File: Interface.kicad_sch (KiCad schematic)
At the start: 14 parts, among them J1 Debugger, J2 USART, J3 SPI, P1 USB_C_Plug_USB2.0

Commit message: change pin default and try layout
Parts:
- removed P1: USB_C_Plug_USB2.0, Connector_USB:USB_C_Receptacle_HRO_TYPE-C-31-M-12, symbol Connector:USB_C_Plug_USB2.0
- removed R10, R9: 20, Resistor_SMD:R_0603_1608Metric, symbol Device:R_Small
- removed R11: 1.5K, Resistor_SMD:R_0603_1608Metric, symbol Device:R_Small
- added J4: USB_C_Receptacle_USB2.0, Connector_USB:USB_C_Receptacle_HRO_TYPE-C-31-M-12, symbol Connector:USB_C_Receptacle_USB2.0
- added U3: USBLC6-2SC6, Package_TO_SOT_SMD:SOT-23-6, symbol Power_Protection:USBLC6-2SC6
- R25: value 0 -> 5.1K
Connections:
- net D+: now also U3.4 (I/O2)
- net D-: now also U3.6 (I/O1)
- net GND: now also J4.A1 (GND), J4.A12 (GND), J4.B1 (GND), J4.B12 (GND), J4.S1 (SHIELD), U3.2 (GND)
- net MISO: now also J3.2 (Pin_2); no longer J3.3 (Pin_3)
- net MOSI: now also J3.3 (Pin_3); no longer J3.4 (Pin_4)
- net SCK: now also J3.4 (Pin_4); no longer J3.2 (Pin_2)
- net VIN: now also J4.A4 (VBUS), J4.A9 (VBUS), J4.B4 (VBUS), J4.B9 (VBUS), U3.5 (VBUS)
- net at R25.1: now also J4.B5 (CC2)
- net at R24.1: now also J4.A5 (CC1)
- new net: J4.A7 (D-), J4.B7 (D-), U3.1 (I/O1)
- new net: J4.A6 (D+), J4.B6 (D+), U3.3 (I/O2)

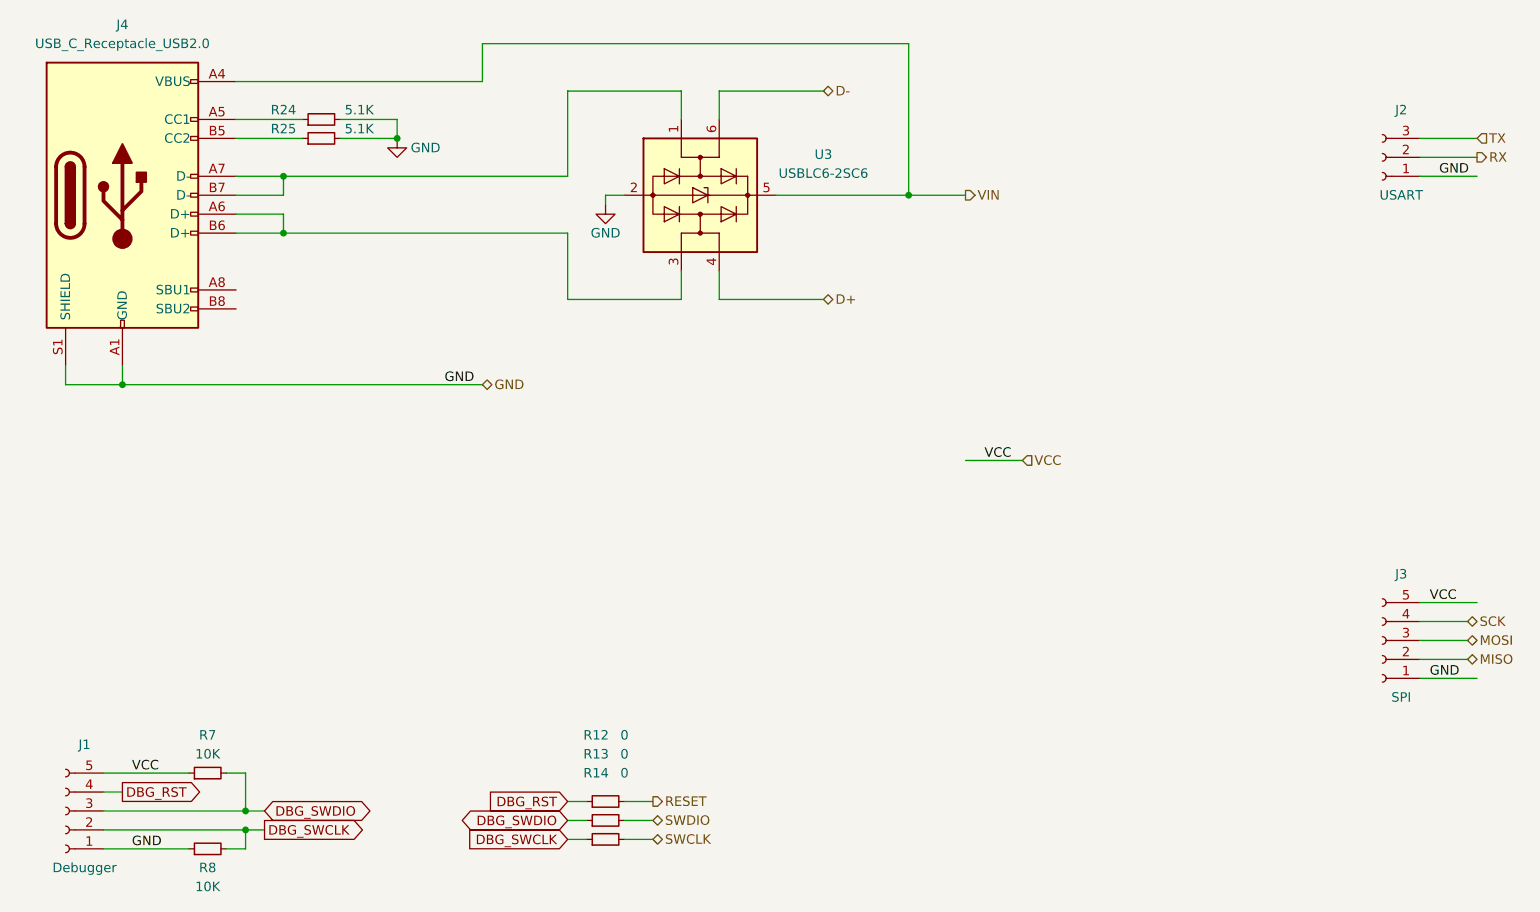
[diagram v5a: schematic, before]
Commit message: add usb enable pin
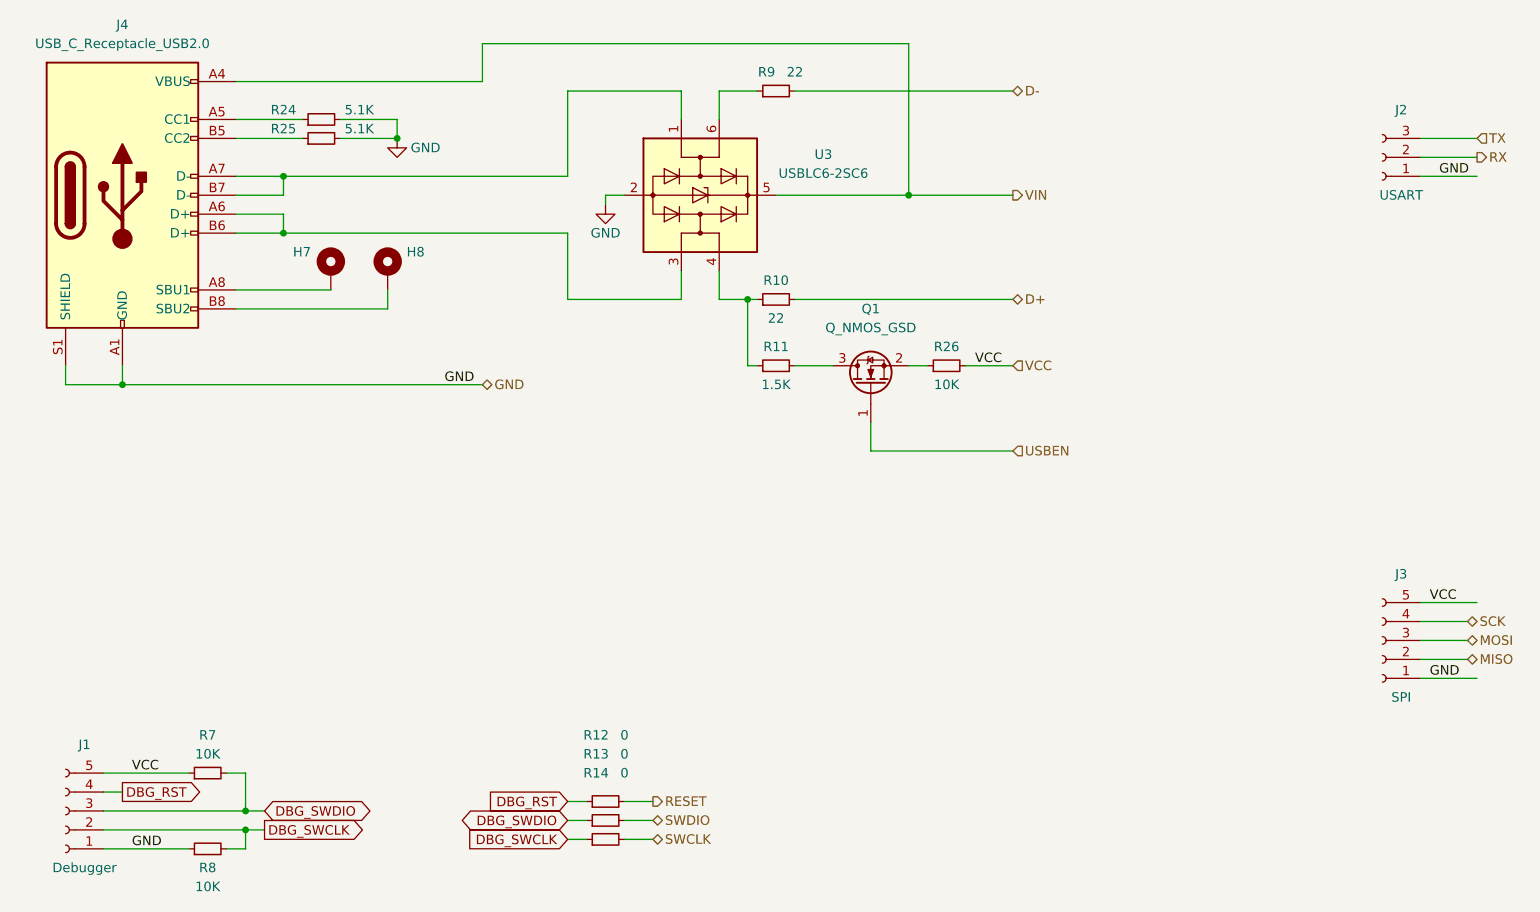
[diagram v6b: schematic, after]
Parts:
- added H7, H8: MountingHole_Pad, NetTie:NetTie-2_SMD_Pad0.5mm, symbol Mechanical:MountingHole_Pad
- added Q1: Q_NMOS_GSD, Package_TO_SOT_SMD:SOT-23, symbol Device:Q_NMOS_GSD
- added R10, R9: 22, Resistor_SMD:R_0603_1608Metric, symbol Device:R_Small
- added R11: 1.5K, Resistor_SMD:R_0603_1608Metric, symbol Device:R_Small
- added R26: 10K, Resistor_SMD:R_0603_1608Metric, symbol Device:R_Small
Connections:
- net D+: now also R10.2; no longer U3.4 (I/O2)
- net D-: now also R9.2; no longer U3.6 (I/O1)
- net VCC: now also R26.2
- net at J4.A8 (SBU1): now also H7.1
- net at J4.B8 (SBU2): now also H8.1
- new net: R10.1, R11.1, U3.4 (I/O2)
- new net: R9.1, U3.6 (I/O1)
- new net: Q1.3 (D), R11.2
- new net: Q1.2 (S), R26.1
- new net USBEN: Q1.1 (G)
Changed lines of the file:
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@@
   (junction (at 77.47 50.8) (diameter 0) (color 0 0 0 0)
   )
+  (junction (at 139.7 67.31) (diameter 0) (color 0 0 0 0)
+  )
   (junction (at 77.47 58.42) (diameter 0) (color 0 0 0 0)
   )
@@
     (stroke (width 0) (type default) (color 0 0 0 0))
   )
+  (wire (pts (xy 139.7 76.2) (xy 139.7 67.31))
+    (stroke (width 0) (type default) (color 0 0 0 0))
+  )
   (wire (pts (xy 130.81 67.31) (xy 130.81 63.5))
     (stroke (width 0) (type default) (color 0 0 0 0))
@@
     (stroke (width 0) (type default) (color 0 0 0 0))
   )
+  (wire (pts (xy 140.97 76.2) (xy 139.7 76.2))
+    (stroke (width 0) (type default) (color 0 0 0 0))
+  )
   (wire (pts (xy 53.34 140.97) (xy 64.77 140.97))
     (stroke (width 0) (type default) (color 0 0 0 0))
   )
+  (wire (pts (xy 146.05 67.31) (xy 175.26 67.31))
+    (stroke (width 0) (type default) (color 0 0 0 0))
+  )
   (wire (pts (xy 229.87 115.57) (xy 236.22 115.57))
     (stroke (width 0) (type default) (color 0 0 0 0))
@@
     (stroke (width 0) (type default) (color 0 0 0 0))
   )
+  (wire (pts (xy 146.05 39.37) (xy 175.26 39.37))
+    (stroke (width 0) (type default) (color 0 0 0 0))
+  )
+  (wire (pts (xy 156.21 87.63) (xy 156.21 83.82))
+    (stroke (width 0) (type default) (color 0 0 0 0))
+  )
   (wire (pts (xy 123.19 139.7) (xy 127 139.7))
     (stroke (width 0) (type default) (color 0 0 0 0))
@@
     (stroke (width 0) (type default) (color 0 0 0 0))
   )
-  (wire (pts (xy 135.89 67.31) (xy 149.86 67.31))
+  (wire (pts (xy 135.89 67.31) (xy 139.7 67.31))
     (stroke (width 0) (type default) (color 0 0 0 0))
   )
@@
     (stroke (width 0) (type default) (color 0 0 0 0))
   )
+  (wire (pts (xy 71.12 66.04) (xy 83.82 66.04))
+    (stroke (width 0) (type default) (color 0 0 0 0))
+  )
   (wire (pts (xy 229.87 48.26) (xy 237.49 48.26))
     (stroke (width 0) (type default) (color 0 0 0 0))
@@
     (stroke (width 0) (type default) (color 0 0 0 0))
   )
+  (wire (pts (xy 135.89 39.37) (xy 140.97 39.37))
+    (stroke (width 0) (type default) (color 0 0 0 0))
+  )
   (wire (pts (xy 123.19 137.16) (xy 127 137.16))
     (stroke (width 0) (type default) (color 0 0 0 0))
   )
+  (wire (pts (xy 168.91 76.2) (xy 175.26 76.2))
+    (stroke (width 0) (type default) (color 0 0 0 0))
+  )
   (wire (pts (xy 71.12 45.72) (xy 80.01 45.72))
     (stroke (width 0) (type default) (color 0 0 0 0))
@@
     (stroke (width 0) (type default) (color 0 0 0 0))
   )
+  (wire (pts (xy 146.05 76.2) (xy 151.13 76.2))
+    (stroke (width 0) (type default) (color 0 0 0 0))
+  )
+  (wire (pts (xy 175.26 87.63) (xy 156.21 87.63))
+    (stroke (width 0) (type default) (color 0 0 0 0))
+  )
+  (wire (pts (xy 71.12 68.58) (xy 91.44 68.58))
+    (stroke (width 0) (type default) (color 0 0 0 0))
+  )
   (wire (pts (xy 53.34 133.35) (xy 55.88 133.35))
     (stroke (width 0) (type default) (color 0 0 0 0))
   )
-  (wire (pts (xy 161.29 53.34) (xy 168.91 53.34))
+  (wire (pts (xy 161.29 53.34) (xy 175.26 53.34))
     (stroke (width 0) (type default) (color 0 0 0 0))
   )
@@
     (stroke (width 0) (type default) (color 0 0 0 0))
   )
-  (wire (pts (xy 135.89 39.37) (xy 149.86 39.37))
+  (wire (pts (xy 161.29 76.2) (xy 163.83 76.2))
     (stroke (width 0) (type default) (color 0 0 0 0))
   )
@@
     (stroke (width 0) (type default) (color 0 0 0 0))
   )
-  (wire (pts (xy 168.91 88.9) (xy 176.53 88.9))
-    (stroke (width 0) (type default) (color 0 0 0 0))
-  )
   (wire (pts (xy 104.14 33.02) (xy 161.29 33.02))
     (stroke (width 0) (type default) (color 0 0 0 0))
@@
     (stroke (width 0) (type default) (color 0 0 0 0))
   )
+  (wire (pts (xy 91.44 68.58) (xy 91.44 66.04))
+    (stroke (width 0) (type default) (color 0 0 0 0))
+  )
   (wire (pts (xy 123.19 134.62) (xy 127 134.62))
+    (stroke (width 0) (type default) (color 0 0 0 0))
+  )
+  (wire (pts (xy 139.7 67.31) (xy 140.97 67.31))
     (stroke (width 0) (type default) (color 0 0 0 0))
   )
@@
     (effects (font (size 1.27 1.27)) (justify left bottom))
   )
-  (label "VCC" (at 171.45 88.9 0)
+  (label "VCC" (at 170.18 76.2 0)
     (effects (font (size 1.27 1.27)) (justify left bottom))
   )
@@
     )
   )
-  (hierarchical_label "D+" (shape bidirectional) (at 149.86 67.31 0)
+  (hierarchical_label "D+" (shape bidirectional) (at 175.26 67.31 0)
     (effects (font (size 1.27 1.27)) (justify left))
   )
@@
     (effects (font (size 1.27 1.27)) (justify left))
   )
-  (hierarchical_label "VCC" (shape input) (at 176.53 88.9 0)
+  (hierarchical_label "VCC" (shape input) (at 175.26 76.2 0)
     (effects (font (size 1.27 1.27)) (justify left))
   )
@@
     (effects (font (size 1.27 1.27)) (justify left))
   )
-  (hierarchical_label "D-" (shape bidirectional) (at 149.86 39.37 0)
+  (hierarchical_label "D-" (shape bidirectional) (at 175.26 39.37 0)
     (effects (font (size 1.27 1.27)) (justify left))
   )
@@
     (effects (font (size 1.27 1.27)) (justify left))
   )
+  (hierarchical_label "USBEN" (shape input) (at 175.26 87.63 0)
+    (effects (font (size 1.27 1.27)) (justify left))
+  )
   (hierarchical_label "SWCLK" (shape bidirectional) (at 127 139.7 0)
     (effects (font (size 1.27 1.27)) (justify left))
   )
-  (hierarchical_label "VIN" (shape output) (at 168.91 53.34 0)
+  (hierarchical_label "VIN" (shape output) (at 175.26 53.34 0)
     (effects (font (size 1.27 1.27)) (justify left))
   )
@@
     (pin "1")
   )
+  (symbol (lib_id "Mechanical:MountingHole_Pad") (at 83.82 63.5 0) (unit 1)
+    (in_bom yes) (on_board yes)
+    (property "Reference" "H7" (id 0) (at 78.74 60.96 0)
+      (effects (font (size 1.27 1.27)) (justify left))
+    )
+    (property "Value" "MountingHole_Pad" (id 1) (at 86.36 63.4999 0)
+      (effects (font (size 1.27 1.27)) (justify left) hide)
+    )
+    (property "Footprint" "NetTie:NetTie-2_SMD_Pad0.5mm" (id 2) (at 83.82 63.5 0)
+      (effects (font (size 1.27 1.27)) hide)
+    )
+    (property "Datasheet" "~" (id 3) (at 83.82 63.5 0)
+      (effects (font (size 1.27 1.27)) hide)
+    )
+    (pin "1")
+  )
+  (symbol (lib_id "Device:R_Small") (at 143.51 76.2 90) (unit 1)
+    (in_bom yes) (on_board yes)
+    (property "Reference" "R11" (id 0) (at 143.51 73.66 90))
+    (property "Value" "1.5K" (id 1) (at 143.51 78.74 90))
+    (property "Footprint" "Resistor_SMD:R_0603_1608Metric" (id 2) (at 143.51 76.2 0)
+      (effects (font (size 1.27 1.27)) hide)
+    )
+    (property "Datasheet" "~" (id 3) (at 143.51 76.2 0)
+      (effects (font (size 1.27 1.27)) hide)
+    )
+    (pin "1")
+    (pin "2")
+  )
   (symbol (lib_id "Device:R_Small") (at 120.65 139.7 90) (unit 1)
     (in_bom yes) (on_board yes)
@@
     (pin "2")
   )
+  (symbol (lib_id "Device:R_Small") (at 166.37 76.2 90) (unit 1)
+    (in_bom yes) (on_board yes)
+    (property "Reference" "R26" (id 0) (at 166.37 73.66 90))
+    (property "Value" "10K" (id 1) (at 166.37 78.74 90))
+    (property "Footprint" "Resistor_SMD:R_0603_1608Metric" (id 2) (at 166.37 76.2 0)
+      (effects (font (size 1.27 1.27)) hide)
+    )
+    (property "Datasheet" "~" (id 3) (at 166.37 76.2 0)
+      (effects (font (size 1.27 1.27)) hide)
+    )
+    (pin "1")
+    (pin "2")
+  )
   (symbol (lib_id "Connector:Conn_01x05_Female") (at 48.26 135.89 180) (unit 1)
     (in_bom yes) (on_board yes)
@@
     )
     (property "Datasheet" "~" (id 3) (at 120.65 137.16 0)
+      (effects (font (size 1.27 1.27)) hide)
+    )
+    (pin "1")
+    (pin "2")
+  )
+  (symbol (lib_id "Device:R_Small") (at 143.51 39.37 90) (unit 1)
+    (in_bom yes) (on_board yes)
+    (property "Reference" "R9" (id 0) (at 142.24 36.83 90))
+    (property "Value" "22" (id 1) (at 146.05 36.83 90))
+    (property "Footprint" "Resistor_SMD:R_0603_1608Metric" (id 2) (at 143.51 39.37 0)
+      (effects (font (size 1.27 1.27)) hide)
+    )
+    (property "Datasheet" "~" (id 3) (at 143.51 39.37 0)
+      (effects (font (size 1.27 1.27)) hide)
+    )
+    (pin "1")
+    (pin "2")
+  )
+  (symbol (lib_id "Device:R_Small") (at 143.51 67.31 90) (unit 1)
+    (in_bom yes) (on_board yes)
+    (property "Reference" "R10" (id 0) (at 143.51 64.77 90))
+    (property "Value" "22" (id 1) (at 143.51 69.85 90))
+    (property "Footprint" "Resistor_SMD:R_0603_1608Metric" (id 2) (at 143.51 67.31 0)
+      (effects (font (size 1.27 1.27)) hide)
+    )
+    (property "Datasheet" "~" (id 3) (at 143.51 67.31 0)
       (effects (font (size 1.27 1.27)) hide)
     )
@@
     (pin "S1")
   )
+  (symbol (lib_id "Device:Q_NMOS_GSD") (at 156.21 78.74 90) (unit 1)
+    (in_bom yes) (on_board yes) (fields_autoplaced)
+    (property "Reference" "Q1" (id 0) (at 156.21 68.58 90))
+    (property "Value" "Q_NMOS_GSD" (id 1) (at 156.21 71.12 90))
+    (property "Footprint" "Package_TO_SOT_SMD:SOT-23" (id 2) (at 153.67 73.66 0)
+      (effects (font (size 1.27 1.27)) hide)
+    )
+    (property "Datasheet" "~" (id 3) (at 156.21 78.74 0)
+      (effects (font (size 1.27 1.27)) hide)
+    )
+    (pin "1")
+    (pin "2")
+    (pin "3")
+  )
+  (symbol (lib_id "Mechanical:MountingHole_Pad") (at 91.44 63.5 0) (unit 1)
+    (in_bom yes) (on_board yes) (fields_autoplaced)
+    (property "Reference" "H8" (id 0) (at 93.98 60.9599 0)
+      (effects (font (size 1.27 1.27)) (justify left))
+    )
+    (property "Value" "MountingHole_Pad" (id 1) (at 93.98 63.4999 0)
+      (effects (font (size 1.27 1.27)) (justify left) hide)
+    )
+    (property "Footprint" "NetTie:NetTie-2_SMD_Pad0.5mm" (id 2) (at 91.44 63.5 0)
+      (effects (font (size 1.27 1.27)) hide)
+    )
+    (property "Datasheet" "~" (id 3) (at 91.44 63.5 0)
+      (effects (font (size 1.27 1.27)) hide)
+    )
+    (pin "1")
+  )
 )

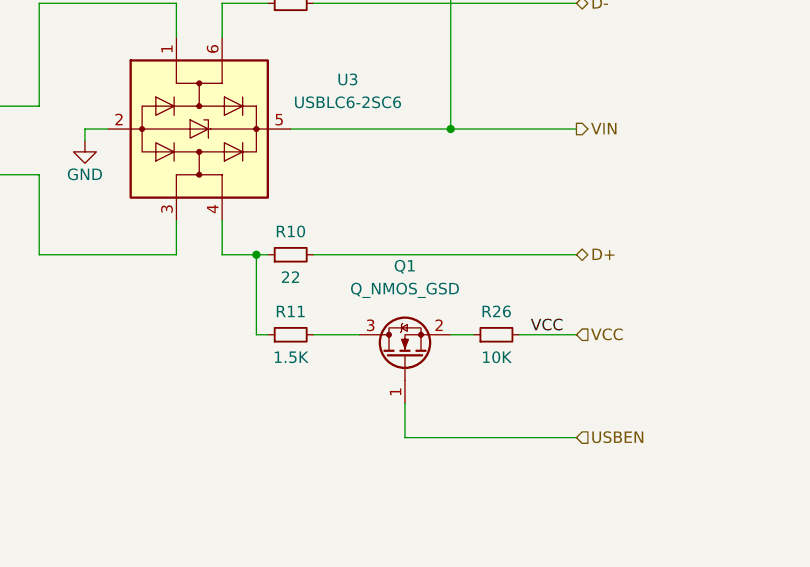
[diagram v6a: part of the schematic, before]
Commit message: update MCU VCC and GND layout
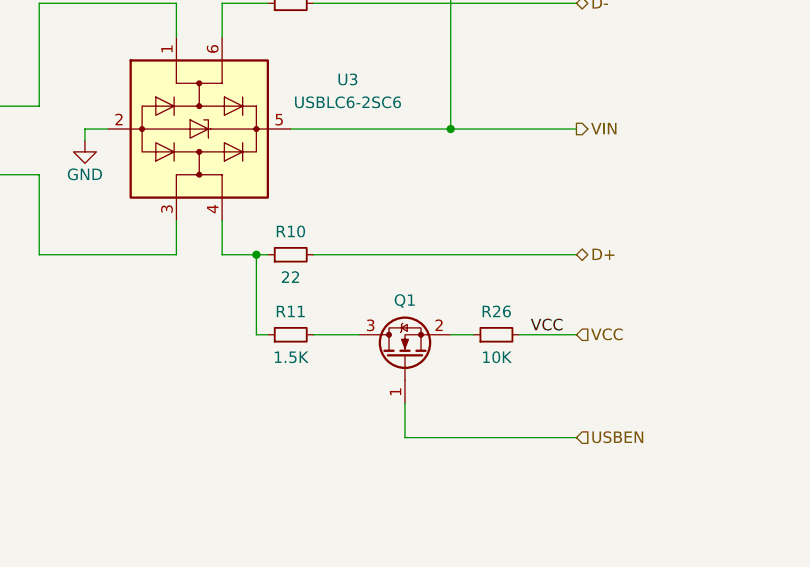
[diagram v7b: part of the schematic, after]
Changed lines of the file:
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@@
   )
   (symbol (lib_id "Device:Q_NMOS_GSD") (at 156.21 78.74 90) (unit 1)
-    (in_bom yes) (on_board yes) (fields_autoplaced)
-    (property "Reference" "Q1" (id 0) (at 156.21 68.58 90))
-    (property "Value" "Q_NMOS_GSD" (id 1) (at 156.21 71.12 90))
+    (in_bom yes) (on_board yes)
+    (property "Reference" "Q1" (id 0) (at 156.21 72.39 90))
+    (property "Value" "Q_NMOS_GSD" (id 1) (at 156.21 71.12 90)
+      (effects (font (size 1.27 1.27)) hide)
+    )
     (property "Footprint" "Package_TO_SOT_SMD:SOT-23" (id 2) (at 153.67 73.66 0)
       (effects (font (size 1.27 1.27)) hide)
